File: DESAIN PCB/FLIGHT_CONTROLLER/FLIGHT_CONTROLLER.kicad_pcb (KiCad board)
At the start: 2 copper layers, 43 parts, among them J1 POWER CONNECTOR, J10 ESC INPUT, J11 ESC INPUT, J12 RC TRANSMITTER, J13 TRANSMITTER, J14 GY-88A, J2 SPI CONNECTOR, J3 USB B, J4 ESC INPUT, J5 ESC INPUT, J6 ESC POWER, J7 ESC POWER, J8 ESC POWER, J9 ESC POWER, SW1 SW_DPDT_x2, SW2 RESET BUTTON, U1 ATmega328P-A, U2 AMS1117-5.0, U3 FT232RL, Y1 16MHz

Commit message: add PCB file
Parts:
- C1, C10, C11, C12, C13, C14, C2, C3, C4, C5, C6, C7, C8, C9, D1, D2, D3, D4, F1, F2, R1, R2, R3, U1, U2, U3: moved to B.Cu
- J2: value SPI CONNECTOR -> SPI PROG
- moved J6 87.8 mm to (177.8, 68.6), turned to 180 degrees
- moved J7 68.6 mm to (104.1, 137.8)
- moved J8 64.1 mm to (172.7, 137.2)
- moved J10 63.1 mm to (172.0, 104.1), turned to -90 degrees
- moved J1 58.9 mm to (137.6, 136.9)
- moved C14 58.4 mm to (163.8, 72.5)
- moved R3 56.1 mm to (170.1, 78.3)
- moved C2 54.2 mm to (148.9, 126.2), turned to 90 degrees
- moved Y1 48.9 mm to (153.7, 105.6), turned to 90 degrees
- moved C1 46.2 mm to (133.3, 102.9), turned to -90 degrees
- moved U1 43.2 mm to (141.2, 102.9), turned to 180 degrees
- moved R1 42.4 mm to (145.3, 82.7)
- moved SW2 42.3 mm to (112.1, 87.6), turned to 90 degrees
- moved J13 41.6 mm to (158.2, 87.4), turned to -90 degrees
- moved F1 40.1 mm to (129.5, 137.2), turned to 90 degrees
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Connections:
- C11 pad 1: VBUS -> +5V
- C12 pad 1: VBUS -> +5V
- C13 pad 1: VBUS -> +5V
- J13 pad 2: /UART_- -> +5V
- J13 pad 4: +5V -> /UART_-
- J2 pad 10: +5V -> GND
- J2 pad 2: unconnected-(J2-Pad2) -> +5V
- J2 pad 3: /RESET -> unconnected-(J2-Pad3)
- J2 pad 4: /SCK -> GND
- J2 pad 5: /MISO -> /RESET
- J2 pad 7: GND -> /SCK
- J2 pad 9: GND -> /MISO
- R2 pad 2: VBUS -> +5V
- R3 pad 2: VBUS -> +5V
- U1 pad 14: /SS -> /D10
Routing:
- net /RESET: track 0.00 -> 137.7 mm, vias 0 -> 2
- net GND: track 0.00 -> 127.8 mm, vias 0 -> 9
- net +5V: track 0.00 -> 73.6 mm, vias 0 -> 8
- net /MOSI: track 0.00 -> 67.9 mm
- net /MISO: track 0.00 -> 66.7 mm
- net /SCK: track 0.00 -> 61.4 mm, vias 0 -> 2
- net /D9: track 0.00 -> 61.2 mm
- net /D10: track 0.00 -> 58.1 mm
- net /D2: track 0.00 -> 55.0 mm
- net /D4: track 0.00 -> 52.7 mm
- net /DATA_+: track 0.00 -> 38.7 mm
- net /DATA_-: track 0.00 -> 38.5 mm
- net /UART_+: track 0.00 -> 32.2 mm
- net /UART_-: track 0.00 -> 31.5 mm
- net /I2C_+: track 0.00 -> 22.5 mm
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- added copper zone on B.Cu, net +5V
- added copper zone on B.Cu, net +BATT
- added copper zone on B.Cu, net GND
- added copper zone on B.Cu, net Net-(F1-Pad1)
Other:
- board text added: "JANGAN LUPA DIBERI SPACER PADA IMU"
- board text added: "PERIKSA KONEKSI"

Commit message: [Board] almost complete
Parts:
- added H1: MountingHole, MountingHole:MountingHole_3.2mm_M3_ISO14580_Pad, F.Cu at (103.6, 79.1)
- added H2: MountingHole, MountingHole:MountingHole_3.2mm_M3_ISO14580_Pad, F.Cu at (178.7, 79.2)
- added H3: MountingHole, MountingHole:MountingHole_3.2mm_M3_ISO14580_Pad, F.Cu at (178.7, 126.6)
- added H4: MountingHole, MountingHole:MountingHole_3.2mm_M3_ISO14580_Pad, F.Cu at (103.6, 126.6)
- added J15: FTDI BREAKOUT BOARD, Connector_PinHeader_2.54mm:PinHeader_1x06_P2.54mm_Vertical, F.Cu at (162.6, 85.1)
- added J16: ESC POWER, TerminalBlock_Phoenix:TerminalBlock_Phoenix_MKDS-1,5-2-5.08_1x02_P5.08mm_Horizontal, F.Cu at (146.6, 137.9)
- moved F1 6.86 mm to (122.7, 137.2)
- moved J1 6.60 mm to (131.0, 136.9)
- moved J13 2.72 mm to (158.2, 90.2)
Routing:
- net +5V: track 73.6 -> 119.7 mm, vias 8 -> 13
- net GND: track 127.8 -> 159.9 mm, vias 9 -> 18
- net VCC: track 15.7 -> 0.00 mm, vias 0 -> 6
- net +BATT: track 13.6 -> 0.00 mm
- net /UART_+: track 32.2 -> 45.1 mm
- net /UART_-: track 31.5 -> 42.1 mm
- net /RESET: track 137.7 -> 139.0 mm
- net /MOSI: track 67.9 -> 68.5 mm
- added copper zone on F.Cu, net +5V
- added copper zone on F.Cu, net GND
- added copper zone on B.Cu, net VCC
- added copper zone on F.Cu, net VCC
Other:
- board outline added: 82.9 x 83.1 mm
- board text removed: "JANGAN LUPA DIBERI SPACER PADA IMU"

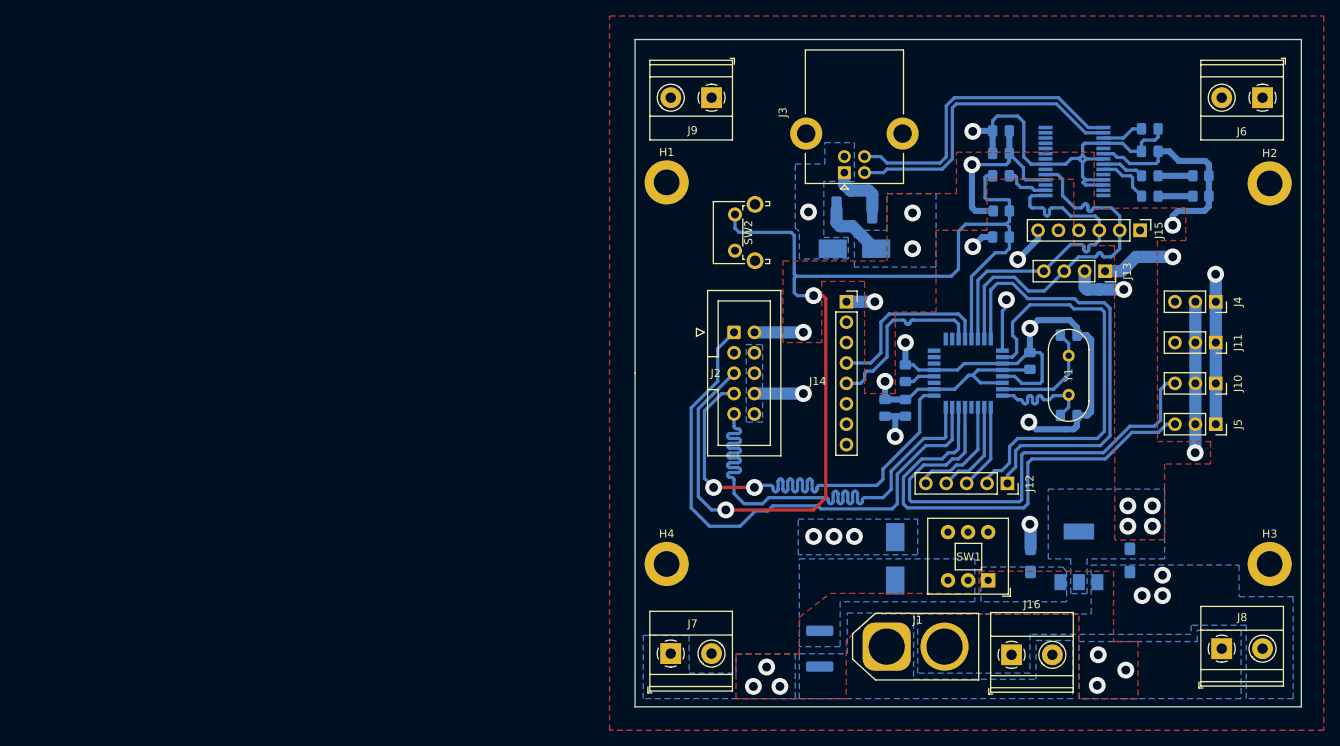
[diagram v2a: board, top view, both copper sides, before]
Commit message: [Broad] just need to route PWM signal
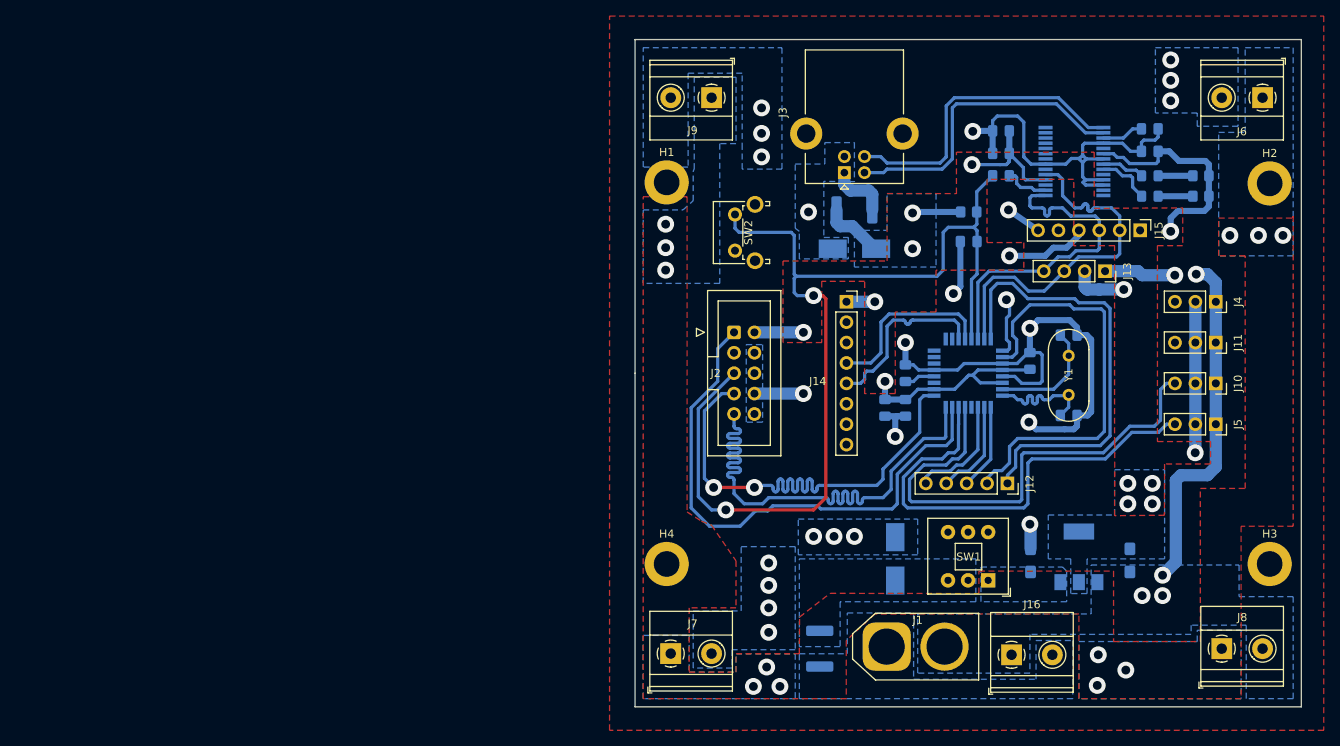
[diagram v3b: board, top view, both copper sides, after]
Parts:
- moved R1 4.07 mm to (141.2, 82.8)
- moved C4 4.06 mm to (141.2, 86.5)
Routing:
- net GND: track 159.9 -> 188.5 mm, vias 18 -> 28
- net /RESET: track 139.0 -> 129.6 mm
- net +5V: track 119.7 -> 128.8 mm, vias 13 -> 14
- net /D3: track 6.55 -> 7.56 mm
- net /UART_-: track 42.1 -> 41.3 mm
- net VCC: vias 6 -> 12

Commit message: [Board] complete, need review
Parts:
- moved J4 12.9 mm to (172.0, 106.8)
- moved J5 10.1 mm to (172.0, 99.1)
- moved J10 7.72 mm to (172.0, 96.4)
- moved J11 5.11 mm to (172.0, 104.2)
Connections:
- J11 pad 3: /D11 -> /MOSI
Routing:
- net /D3: track 7.56 -> 56.8 mm, vias 1 -> 2
- net /MOSI: track 68.5 -> 115.7 mm
- net /D10: track 58.1 -> 67.0 mm
- net /D9: track 61.2 -> 67.5 mm
- net +5V: track 128.8 -> 126.4 mm
- net /D4: track 52.4 -> 50.9 mm
- net /D2: track 55.5 -> 53.9 mm
- net /UART_+: track 44.9 -> 44.2 mm
- net /UART_-: track 41.3 -> 41.9 mm
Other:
- board text added: "====>"
- board text added: "MOTOR X ==> D03"
- board text added: "MOTOR X ==> D09"
- board text added: "MOTOR X ==> D10"
- board text added: "MOTOR X ==> D11"

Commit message: [Board] Review complete
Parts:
- added kibuzzard-63DE9C89: G***, kibuzzard-63DE9C89, F.Cu at (148.6, 119.8)
- added kibuzzard-63DE9C99: G***, kibuzzard-63DE9C99, F.Cu at (151.1, 119.8)
- added kibuzzard-63DE9E57: G***, kibuzzard-63DE9E57, F.Cu at (146.2, 113.3)
- added kibuzzard-63DE9E82: G***, kibuzzard-63DE9E82, F.Cu at (143.5, 113.0)
- added kibuzzard-63DE9F2F: G***, kibuzzard-63DE9F2F, F.Cu at (141.1, 112.8)
- added kibuzzard-63DE9F75: G***, kibuzzard-63DE9F75, F.Cu at (138.4, 113.2)
- added kibuzzard-63DE9FCF: G***, kibuzzard-63DE9FCF, F.Cu at (135.9, 113.3)
- added kibuzzard-63DEA0F2: G***, kibuzzard-63DEA0F2, F.Cu at (169.4, 109.7)
- added kibuzzard-63DEA114: G***, kibuzzard-63DEA114, F.Cu at (161.3, 106.8)
- added kibuzzard-63DEA11E: G***, kibuzzard-63DEA11E, F.Cu at (161.3, 104.1)
- added kibuzzard-63DEA12D: G***, kibuzzard-63DEA12D, F.Cu at (161.2, 99.1)
- added kibuzzard-63DEA138: G***, kibuzzard-63DEA138, F.Cu at (161.2, 96.4)
- J12: footprint Connector_PinSocket_2.54mm:PinSocket_1x05_P2.54mm_Vertical -> Connector_PinSocket_2.54mm:PinSocket_1x07_P2.54mm_Vertical
- J15: footprint Connector_PinHeader_2.54mm:PinHeader_1x06_P2.54mm_Vertical -> Connector_PinSocket_2.54mm:PinSocket_1x06_P2.54mm_Vertical
- moved J12 5.08 mm to (151.1, 116.6)
- moved J16 0.58 mm to (146.6, 137.3)
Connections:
- net /MOSI renamed /D11
- J12 pad 1: /D2 -> GND
- J12 pad 2: /D4 -> +5V
- J12 pad 3: /D5 -> /D2
- J12 pad 4: /D6 -> /D4
- J12 pad 5: /D7 -> /D5
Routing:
- net +5V: track 126.4 -> 182.5 mm, vias 14 -> 15
- net GND: track 189.0 -> 201.3 mm, vias 28 -> 30
- net /D3: track 56.8 -> 63.5 mm
- net /D2: track 53.9 -> 56.2 mm
- net /D9: track 67.5 -> 69.0 mm
- net /D10: track 67.0 -> 68.5 mm
- net /D11: track 115.7 -> 116.9 mm
- net /D4: track 50.9 -> 51.9 mm
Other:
- board text added: "TRIK FLIGHT CONTROLLER DESIGN BY : ALIM SATRIA"

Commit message: [board] complete
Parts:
- added kibuzzard-63E0D02C: G***, kibuzzard-63E0D02C, F.Cu at (141.6, 102.9)
- added kibuzzard-63E0D05B: G***, kibuzzard-63E0D05B, B.Cu at (141.0, 64.8)
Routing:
- net GND: track 201.3 -> 198.7 mm, vias 30 -> 31
- net /UART_-: track 41.9 -> 43.3 mm
- net /RESET: track 129.2 -> 128.4 mm
- net +5V: track 182.5 -> 181.7 mm
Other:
- board text removed: "====>"
